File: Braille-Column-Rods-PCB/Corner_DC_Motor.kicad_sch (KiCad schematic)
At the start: 9 parts, among them M12 Motor_DC_With_MP, U13 AD116, U28 MT910xET

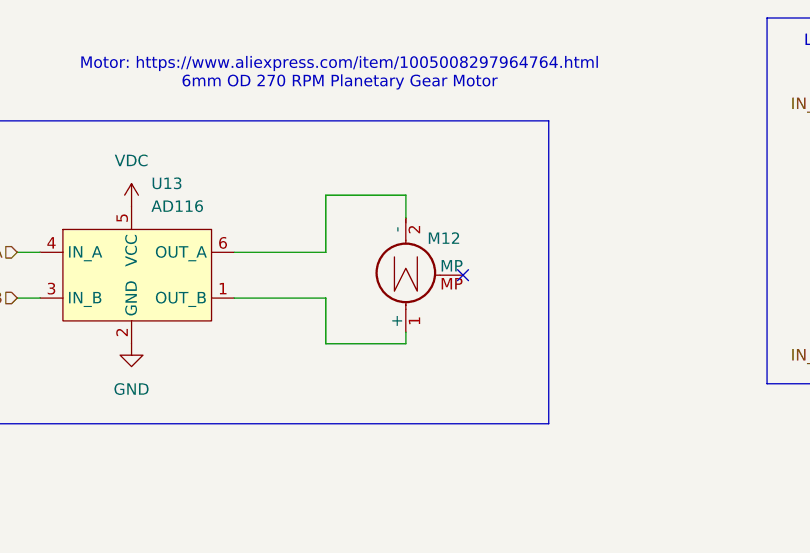
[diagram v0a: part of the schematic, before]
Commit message: Fix dimension issues with stepper motor
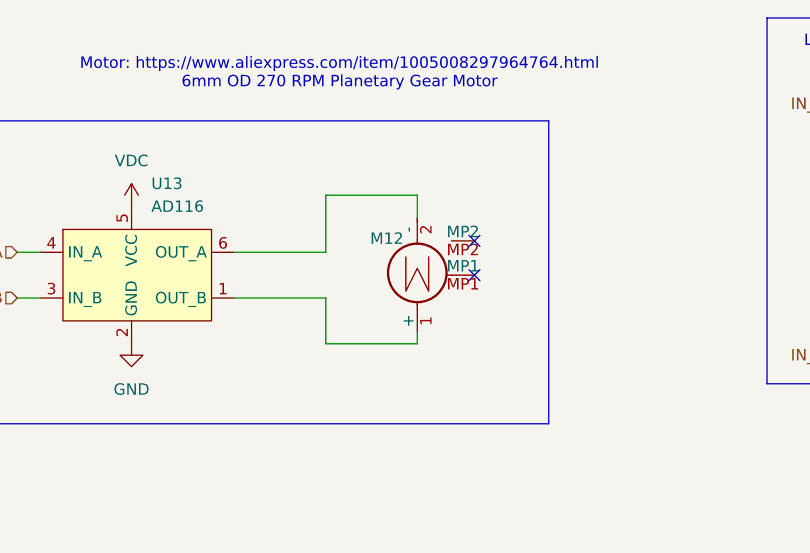
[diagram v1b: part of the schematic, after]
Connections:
- no-connect marks 1 -> 2
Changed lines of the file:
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@@
 	)
 	(no_connect
-		(at 143.51 71.12)
+		(at 144.78 67.31)
+	)
+	(no_connect
+		(at 144.78 71.12)
 	)
 	(wire
@@
 	(wire
 		(pts
-			(xy 128.27 78.74) (xy 137.16 78.74)
+			(xy 128.27 78.74) (xy 138.43 78.74)
 		)
 		(stroke
@@
 	(wire
 		(pts
-			(xy 137.16 64.77) (xy 137.16 62.23)
+			(xy 138.43 64.77) (xy 138.43 62.23)
 		)
 		(stroke
@@
 	(wire
 		(pts
-			(xy 137.16 62.23) (xy 128.27 62.23)
+			(xy 138.43 62.23) (xy 128.27 62.23)
 		)
 		(stroke
@@
 	(wire
 		(pts
-			(xy 137.16 78.74) (xy 137.16 77.47)
+			(xy 138.43 78.74) (xy 138.43 77.47)
 		)
 		(stroke
@@
 		(shape input)
 		(at 93.98 68.58 180)
-		(fields_autoplaced yes)
 		(effects
 			(font
@@
 		(shape output)
 		(at 234.95 144.78 0)
-		(fields_autoplaced yes)
 		(effects
 			(font
@@
 		(shape input)
 		(at 93.98 73.66 180)
-		(fields_autoplaced yes)
 		(effects
 			(font
@@
 		(shape input)
 		(at 185.42 80.01 180)
-		(fields_autoplaced yes)
 		(effects
 			(font
@@
 		(shape input)
 		(at 185.42 52.07 180)
-		(fields_autoplaced yes)
 		(effects
 			(font
@@
 	(symbol
 		(lib_id "00-lib-symbols:Motor_DC_With_MP")
-		(at 137.16 72.39 180)
+		(at 138.43 72.39 180)
 		(unit 1)
 		(exclude_from_sim no)
@@
 		(dnp no)
 		(property "Reference" "M12"
-			(at 143.256 67.056 0)
+			(at 136.906 67.056 0)
 			(effects
 				(font
@@
 		)
 		(property "Value" "Motor_DC_With_MP"
-			(at 156.972 65.532 0)
+			(at 158.242 65.532 0)
 			(effects
 				(font
@@
 		)
 		(property "Footprint" "00-lib-footprints:DC_Motor_6mm_OD_with_3_Stage_Gearbox"
-			(at 137.16 70.104 0)
+			(at 138.43 70.104 0)
 			(effects
 				(font
@@
 		)
 		(property "Datasheet" "~"
-			(at 137.16 70.104 0)
+			(at 138.43 70.104 0)
 			(effects
 				(font
@@
 		)
 		(property "Description" "DC Motor"
-			(at 137.16 72.39 0)
+			(at 138.43 72.39 0)
 			(effects
 				(font
@@
 		(pin "2"
 		)
-		(pin "MP"
+		(pin "MP1"
+		)
+		(pin "MP2"
 		)
 		(instances

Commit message: Polish prep for Rev 2 release, PCBA work
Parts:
- U13: value AD116 -> AD116_or_BDR6120S; symbol 00-project-symbols:AD116_H_Bridge -> 00-lib-symbols:AD116_H_Bridge; LCSC (none) -> C5455570
- U28: value MT910xET -> MT9101ET; LCSC (none) -> C2977713
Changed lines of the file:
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@@
 	(title_block
 		(title "Braille Cam Rod Prototype (Type 4)")
-		(date "2025-01-06")
-		(rev "Rev 1")
+		(date "2025-02-03")
+		(rev "Rev 2")
 	)
 	(junction
@@
 	(wire
 		(pts
-			(xy 118.11 68.58) (xy 128.27 68.58)
+			(xy 118.11 68.58) (xy 129.54 68.58)
 		)
 		(stroke
@@
 	(wire
 		(pts
-			(xy 128.27 78.74) (xy 138.43 78.74)
+			(xy 129.54 78.74) (xy 138.43 78.74)
 		)
 		(stroke
@@
 	(wire
 		(pts
-			(xy 118.11 73.66) (xy 128.27 73.66)
+			(xy 118.11 73.66) (xy 129.54 73.66)
 		)
 		(stroke
@@
 	(wire
 		(pts
-			(xy 138.43 62.23) (xy 128.27 62.23)
+			(xy 138.43 62.23) (xy 129.54 62.23)
 		)
 		(stroke
@@
 	(wire
 		(pts
-			(xy 128.27 62.23) (xy 128.27 68.58)
+			(xy 129.54 62.23) (xy 129.54 68.58)
 		)
 		(stroke
@@
 	(wire
 		(pts
-			(xy 128.27 73.66) (xy 128.27 78.74)
+			(xy 129.54 73.66) (xy 129.54 78.74)
 		)
 		(stroke
@@
 			)
 		)
-		(property "Value" "MT910xET"
+		(property "Value" "MT9101ET"
 			(at 218.44 146.0499 0)
 			(effects
@@
 		)
 		(property "Description" ""
+			(at 222.25 144.78 0)
+			(effects
+				(font
+					(size 1.27 1.27)
+				)
+				(hide yes)
+			)
+		)
+		(property "LCSC" "C2977713"
 			(at 222.25 144.78 0)
 			(effects
@@
 	)
 	(symbol
-		(lib_id "00-project-symbols:AD116_H_Bridge")
+		(lib_id "00-lib-symbols:AD116_H_Bridge")
 		(at 106.68 71.12 0)
 		(unit 1)
@@
 			)
 		)
-		(property "Value" "AD116"
+		(property "Value" "AD116_or_BDR6120S"
 			(at 108.8741 63.5 0)
 			(effects
@@
 			(effects
 				(font
+					(size 1.27 1.27)
+				)
+				(hide yes)
+			)
+		)
+		(property "LCSC" "C5455570"
+			(at 106.68 71.12 0)
+			(effects
+				(font

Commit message: chore: bump to KiCAD v8 on re-save
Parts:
- renumbered C13 to C10, C39 to C33, C40 to C34, D15 to D12, D20 to D17, M12 to M9, R41 to R38, U13 to U10, U28 to U25
